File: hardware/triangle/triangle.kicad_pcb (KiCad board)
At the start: 4 copper layers, 100 x 86.6 mm, 63 parts, among them J1 USB_C_Receptacle_USB2.0_16P, J2 USB_C_Receptacle_USB2.0_16P

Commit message: add more power items
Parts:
- added C26: 100nF, Capacitor_SMD:C_0402_1005Metric, B.Cu at (164.6, 117.4)
- added C27: 10µF, Capacitor_SMD:C_0603_1608Metric, B.Cu at (160.1, 120.5)
- added C28: 10µF, Capacitor_SMD:C_0603_1608Metric, B.Cu at (166.2, 113.5)
- added L1: MGFL2012F2R2MT-LF, footprints:L0805, B.Cu at (164.2, 113.9)
- added R3: 100kΩ, Resistor_SMD:R_0402_1005Metric, B.Cu at (167.7, 122.9)
- added R4: 560kΩ, Resistor_SMD:R_0402_1005Metric, B.Cu at (167.9, 121.2)
- added R9: 100kΩ, Resistor_SMD:R_0402_1005Metric, B.Cu at (162.5, 122.0)
- added U2: EA8212HT6R, footprints:SOT-23-6_L2.9-W1.6-P0.95-LS2.8-BR, B.Cu at (164.4, 119.8)
- renumbered TP1-5V1 to TP1-4V1, TP3_LED_DATA_OUT to TP3-LED_DATA_OUT1
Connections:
- net 5V Power renamed 4V Power
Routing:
- net 4V Power: track 98.2 -> 110.0 mm, vias 25 -> 27
- net 12V Power: track 16.5 -> 24.5 mm, vias 4 -> 5
- net GND: track 95.9 -> 101.7 mm, vias 24 -> 28
- net Net-(U2-SWITCH): track 0.00 -> 4.27 mm
- net Net-(U2-FBK): track 0.00 -> 3.44 mm
- net Net-(U2-BOOT): track 0.00 -> 1.62 mm
- net Net-(U2-RUN): track 0.00 -> 1.25 mm

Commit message: trying to fix schematic
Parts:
- turned R3 to 0 degrees
- turned R4 to 0 degrees
- turned R9 to 180 degrees
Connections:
- C1 pad 1: 4V Power -> +4V
- C10 pad 1: 4V Power -> +4V
- C11 pad 1: 4V Power -> +4V
- C12 pad 1: 4V Power -> +4V
- C13 pad 1: 4V Power -> +4V
- C14 pad 1: 4V Power -> +4V
- C15 pad 1: 4V Power -> +4V
- C16 pad 1: 4V Power -> +4V
- C17 pad 1: 4V Power -> +4V
- C18 pad 1: 4V Power -> +4V
- C19 pad 1: 4V Power -> +4V
- C2 pad 1: 4V Power -> +4V
- C20 pad 1: 4V Power -> +4V
- C21 pad 1: 4V Power -> +4V
- C22 pad 1: 4V Power -> +4V
- C23 pad 1: 4V Power -> +4V
- C24 pad 1: 4V Power -> +4V
- C25 pad 2: 12V Power -> +12V
- C27 pad 1: 12V Power -> +12V
- C28 pad 1: 4V Power -> +4V
- C3 pad 1: 4V Power -> +4V
- C4 pad 1: 4V Power -> +4V
- C5 pad 1: 4V Power -> +4V
- C6 pad 1: 4V Power -> +4V
- C7 pad 1: 4V Power -> +4V
- C8 pad 1: 4V Power -> +4V
- C9 pad 1: 4V Power -> +4V
- D1 pad 4: 4V Power -> +4V
- D10 pad 4: 4V Power -> +4V
- D11 pad 4: 4V Power -> +4V
- D12 pad 4: 4V Power -> +4V
- D13 pad 4: 4V Power -> +4V
- D14 pad 4: 4V Power -> +4V
- D15 pad 4: 4V Power -> +4V
- D16 pad 4: 4V Power -> +4V
- D17 pad 4: 4V Power -> +4V
- D18 pad 4: 4V Power -> +4V
- D19 pad 4: 4V Power -> +4V
- D2 pad 4: 4V Power -> +4V
- D20 pad 4: 4V Power -> +4V
- D21 pad 4: 4V Power -> +4V
- D22 pad 4: 4V Power -> +4V
- D23 pad 4: 4V Power -> +4V
- D24 pad 4: 4V Power -> +4V
- D3 pad 4: 4V Power -> +4V
- D4 pad 4: 4V Power -> +4V
- D5 pad 4: 4V Power -> +4V
- D6 pad 4: 4V Power -> +4V
- D7 pad 4: 4V Power -> +4V
- D8 pad 4: 4V Power -> +4V
- D9 pad 4: 4V Power -> +4V
- J1 pad A4: 12V Power -> +12V
- J1 pad A9: 12V Power -> +12V
- J1 pad B4: 12V Power -> +12V
- J1 pad B9: 12V Power -> +12V
- J2 pad A4: 12V Power -> +12V
- J2 pad A9: 12V Power -> +12V
- J2 pad B4: 12V Power -> +12V
- J2 pad B9: 12V Power -> +12V
- L1 pad 2: 4V Power -> +4V
- R3 pad 1: GND -> Net-(U2-FBK)
- R3 pad 2: Net-(U2-FBK) -> GND
- R4 pad 1: 4V Power -> Net-(U2-FBK)
- R4 pad 2: Net-(U2-FBK) -> +4V
- R9 pad 1: 12V Power -> Net-(U2-RUN)
- R9 pad 2: Net-(U2-RUN) -> +12V
- TP1-4V1 pad 1: 4V Power -> unconnected-(TP1-4V1-Pad1)
- U2 pad 5: 12V Power -> +12V
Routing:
- net 4V Power: track 110.0 -> 0.00 mm, vias 27 -> 0
- net +4V: track 0.00 -> 107.8 mm, vias 0 -> 26
- net 12V Power: track 24.5 -> 0.00 mm, vias 5 -> 0
- net +12V: track 0.00 -> 24.5 mm, vias 0 -> 5
- net unconnected-(TP1-4V1-Pad1): track 0.00 -> 2.22 mm, vias 0 -> 1
- added copper zone on In2.Cu, net +12V
- added copper zone on In2.Cu, net +4V
- removed copper zone on In2.Cu, net 12V Power
- removed copper zone on In2.Cu, net 4V Power

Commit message: adjust placement
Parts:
- moved R7 24.2 mm to (154.0, 103.4), turned to 90 degrees
- moved J2 19.3 mm to (149.9, 101.8), turned to 90 degrees
- moved R8 15.6 mm to (146.0, 100.2), turned to -90 degrees
- moved C25 14.0 mm to (132.7, 136.1), turned to 30 degrees
- moved C27 11.2 mm to (167.5, 129.0), turned to -60 degrees
- moved R9 10.5 mm to (170.3, 129.0), turned to -150 degrees
- moved J1 9.83 mm to (132.5, 131.0), turned to -150 degrees
- moved R6 9.07 mm to (137.8, 132.6), turned to -150 degrees
- moved U2 9.03 mm to (170.8, 126.1), turned to 30 degrees
- moved R5 9.02 mm to (130.4, 125.9), turned to -60 degrees
- moved R3 8.69 mm to (175.2, 127.2), turned to 30 degrees
- moved C26 8.39 mm to (169.8, 124.0), turned to -150 degrees
- moved L1 8.05 mm to (167.7, 121.1), turned to 120 degrees
- moved R4 7.99 mm to (174.6, 125.6), turned to 30 degrees
- moved C28 6.98 mm to (169.3, 119.8), turned to -60 degrees
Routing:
- net LED_DATA_OUT: track 54.3 -> 64.4 mm
- net GND: track 101.7 -> 104.8 mm
- net +12V: track 24.5 -> 26.5 mm
- net LED_DATA_IN: track 52.9 -> 54.9 mm

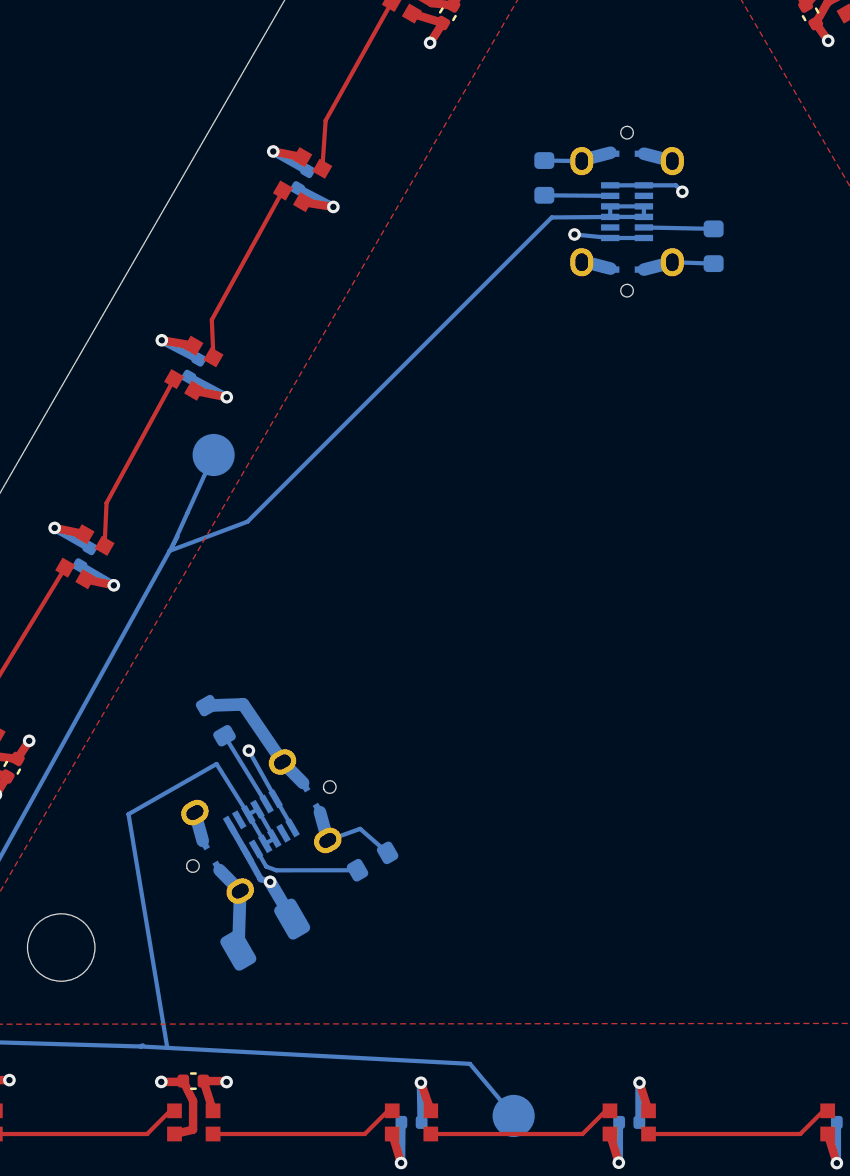
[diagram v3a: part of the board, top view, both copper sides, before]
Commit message: more placement adjustment
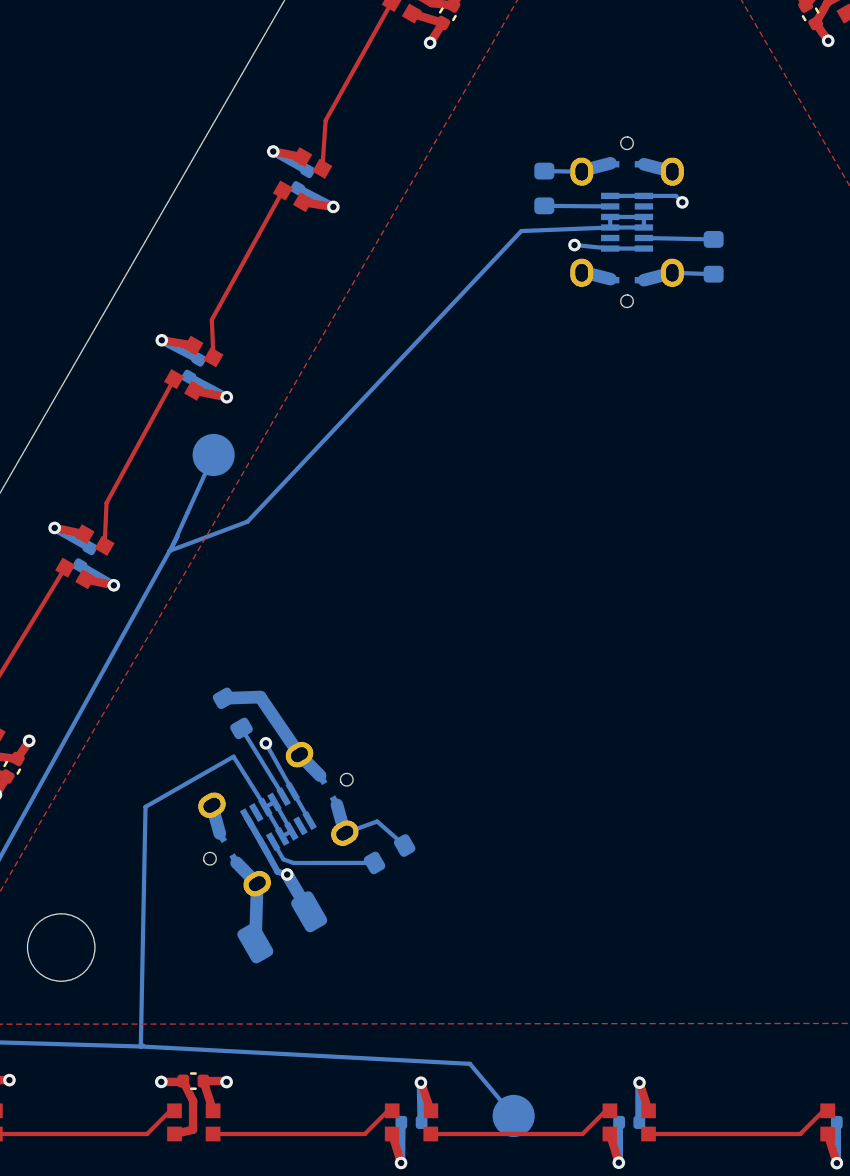
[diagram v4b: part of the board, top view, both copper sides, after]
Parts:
- moved C25 0.88 mm to (133.5, 135.7)
- moved J1 0.88 mm to (133.3, 130.6)
- moved R5 0.88 mm to (131.2, 125.6)
- moved R6 0.88 mm to (138.6, 132.3)
- moved J2 0.50 mm to (149.9, 102.3)
- moved R7 0.50 mm to (154.0, 103.9)
- moved R8 0.50 mm to (146.0, 100.7)

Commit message: more moving things around
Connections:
- TP1-4V1 pad 1: unconnected-(TP1-4V1-Pad1) -> +4V
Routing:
- net unconnected-(TP1-4V1-Pad1): track 2.22 -> 0.00 mm, vias 1 -> 0
- net +4V: track 107.8 -> 109.8 mm, vias 26 -> 27
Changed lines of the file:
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@@
 		)
 		(pad "0" thru_hole oval
-			(at -2.4 -2.15 300)
+			(at -2.4 -2.15 120)
 			(size 1.1 1.35)
 			(drill oval 0.6 0.85)
@@
 		)
 		(pad "0" thru_hole oval
-			(at -2.4 2.15 300)
+			(at -2.4 2.15 120)
 			(size 1.1 1.35)
 			(drill oval 0.6 0.85)
@@
 		)
 		(pad "0" thru_hole oval
-			(at 2.4 -2.15 300)
+			(at 2.4 -2.15 120)
 			(size 1.1 1.35)
 			(drill oval 0.6 0.85)
@@
 		)
 		(pad "0" thru_hole oval
-			(at 2.4 2.15 300)
+			(at 2.4 2.15 120)
 			(size 1.1 1.35)
 			(drill oval 0.6 0.85)
@@
 			(size 2 2)
 			(layers "B.Cu" "B.Mask")
-			(net "unconnected-(TP1-4V1-Pad1)")
+			(net "+4V")
 			(pinfunction "1_1")
 			(pintype "passive")
@@
 		)
 		(pad "0" thru_hole oval
-			(at -2.4 -2.15 180)
+			(at -2.4 -2.15)
 			(size 1.1 1.35)
 			(drill oval 0.6 0.85)
@@
 		)
 		(pad "0" thru_hole oval
-			(at -2.4 2.15 180)
+			(at -2.4 2.15)
 			(size 1.1 1.35)
 			(drill oval 0.6 0.85)
@@
 		)
 		(pad "0" thru_hole oval
-			(at 2.4 -2.15 180)
+			(at 2.4 -2.15)
 			(size 1.1 1.35)
 			(drill oval 0.6 0.85)
@@
 		)
 		(pad "0" thru_hole oval
-			(at 2.4 2.15 180)
+			(at 2.4 2.15)
 			(size 1.1 1.35)
 			(drill oval 0.6 0.85)
@@
 	)
 	(segment
-		(start 128.074531 141.462226)
-		(end 126.81671 141.395875)
-		(width 0.2)
-		(layer "B.Cu")
-		(net "LED_DATA_IN")
-	)
-	(segment
 		(start 144.514424 144.692369)
 		(end 142.44088 142.220066)
@@
 	)
 	(segment
-		(start 126.902527 141.338451)
-		(end 126.81671 141.395875)
-		(width 0.2)
-		(layer "B.Cu")
-		(net "LED_DATA_IN")
-	)
-	(segment
-		(start 136.287519 141.89547)
-		(end 128.074531 141.462226)
+		(start 126.81671 141.395875)
+		(end 142.44088 142.220066)
 		(width 0.2)
 		(layer "B.Cu")
@@
 	)
 	(segment
-		(start 142.44088 142.220066)
-		(end 136.287519 141.89547)
-		(width 0.2)
-		(layer "B.Cu")
-		(net "LED_DATA_IN")
-	)
-	(segment
 		(start 133.962131 131.174908)
 		(end 133.529119 131.424908)
@@
 	)
 	(segment
-		(start 169.165844 143.016837)
-		(end 169.153779 143.004772)
-		(width 0.4)
-		(layer "F.Cu")
-		(net "+4V")
-	)
-	(segment
 		(start 185.31536 136.550304)
 		(end 184.674005 137.439848)
@@
 	)
 	(via
+		(at 164.243976 103.125342)
+		(size 0.6)
+		(drill 0.3)
+		(layers "F.Cu" "B.Cu")
+		(net "+4V")
+	)
+	(via
 		(at 154.079645 84.77044)
 		(size 0.6)
@@
 	)
 	(segment
-		(start 166.473656 111.591486)
-		(end 166.490384 111.595968)
-		(width 0.6)
+		(start 170.91 109.614192)
+		(end 172.592834 108.71747)
+		(width 0.4)
 		(layer "B.Cu")
 		(net "+4V")
 	)
 	(segment
-		(start 170.91 109.614192)
-		(end 172.592834 108.71747)
-		(width 0.4)
+		(start 165.046119 104.991288)
+		(end 164.243976 103.125342)
+		(width 0.2)
 		(layer "B.Cu")
 		(net "+4V")
@@
 	)
 	(segment
-		(start 169.765236 120.421622)
-		(end 169.701736 120.485122)
-		(width 0.6)
-		(layer "B.Cu")
-		(net "GND")
-	)
-	(segment
 		(start 160.810391 143.089474)
 		(end 160.810391 144.995391)
@@
 	)
 	(segment
-		(start 128.405164 117.472858)
-		(end 128.350952 117.570911)
-		(width 0.2)
-		(layer "B.Cu")
-		(net "LED_DATA_OUT")
-	)
-	(segment
 		(start 149.096593 102.519695)
 		(end 144.879443 102.688609)
@@
 	)
 	(segment
-		(start 128.558578 117.195378)
-		(end 128.405164 117.472858)
-		(width 0.2)
-		(layer "B.Cu")
-		(net "LED_DATA_OUT")
-	)
-	(segment
 		(start 131.88101 116.484287)
 		(end 128.186554 117.868259)
@@
 	)
 	(segment
-		(start 128.350952 117.570911)
-		(end 128.330267 117.608325)
-		(width 0.2)
-		(layer "B.Cu")
-		(net "LED_DATA_OUT")
-	)
-	(segment
-		(start 128.330267 117.608325)
-		(end 128.186554 117.868259)
-		(width 0.2)
-		(layer "B.Cu")
-		(net "LED_DATA_OUT")
-	)
-	(segment
-		(start 129.030734 116.067033)
+		(start 128.186554 117.868259)
 		(end 128.350952 117.570911)
 		(width 0.2)
@@
 	)
 	(segment
-		(start 130.272797 113.31922)
-		(end 129.030734 116.067033)
+		(start 128.350952 117.570911)
+		(end 130.272797 113.31922)
 		(width 0.2)
 		(layer "B.Cu")
@@
 	)
 	(segment
+		(start 167.062539 128.289821)
+		(end 163.215856 128.765665)
+		(width 0.4)
+		(layer "B.Cu")
+		(net "+12V")
+	)
+	(segment
 		(start 149.096593 103.519695)
 		(end 147.402345 103.35256)
@@
 	)
 	(segment
-		(start 167.062539 128.289821)
-		(end 163.6917 128.289821)
-		(width 0.4)
-		(layer "B.Cu")
-		(net "+12V")
-	)
-	(segment
 		(start 149.096593 101.019695)
 		(end 150.696593 101.019695)
@@
 	)
 	(segment
-		(start 163.6917 128.289821)
-		(end 163.215856 128.765665)
-		(width 0.4)
-		(layer "B.Cu")
-		(net "+12V")
-	)
-	(segment
 		(start 132.663093 131.924908)
 		(end 133.310932 133.10203)
@@
 		(net "Net-(J2-CC1)")
 	)
-	(via
-		(at 163.54633 103.350204)
-		(size 0.6)
-		(drill 0.3)
-		(layers "F.Cu" "B.Cu")
-		(net "unconnected-(TP1-4V1-Pad1)")
-	)
-	(segment
-		(start 165.046119 104.991288)
-		(end 163.54633 103.350204)
-		(width 0.4)
-		(layer "B.Cu")
-		(net "unconnected-(TP1-4V1-Pad1)")
-	)
 	(segment
